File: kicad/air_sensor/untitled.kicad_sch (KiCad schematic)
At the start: 7 parts, among them J2 Micro_SD_Card

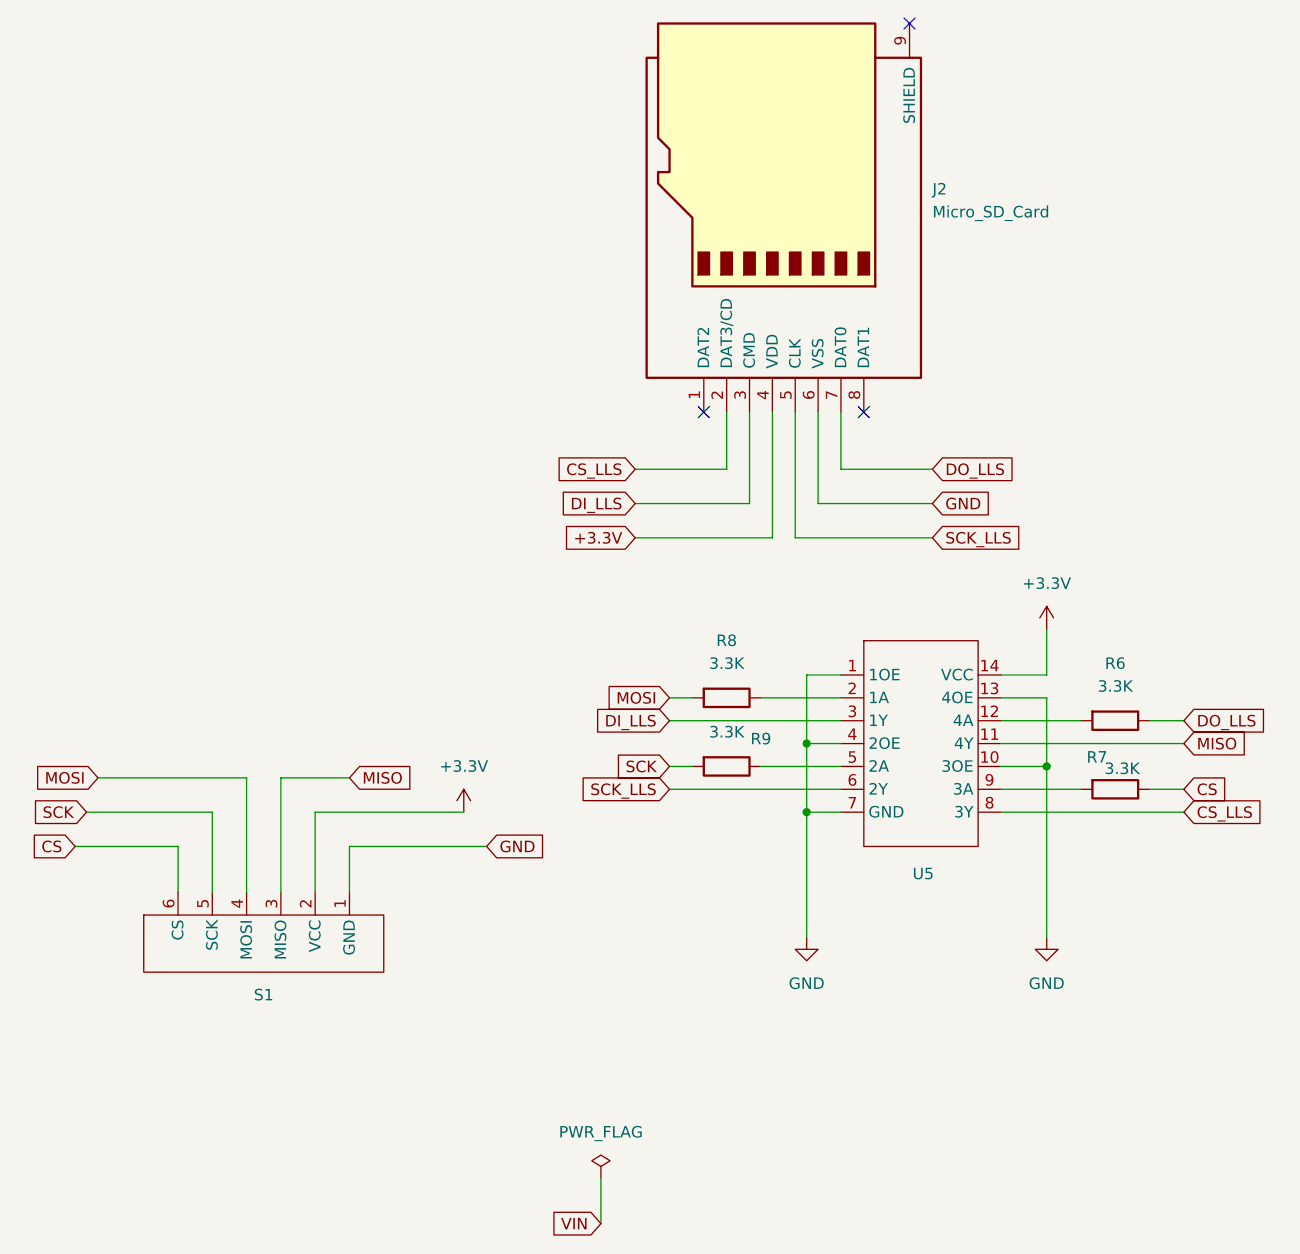
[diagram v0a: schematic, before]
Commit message: updated schema
added 5V 3A buck converter
refined 3v3 LDO
added symbols for new components
added text comments for designing the pcb
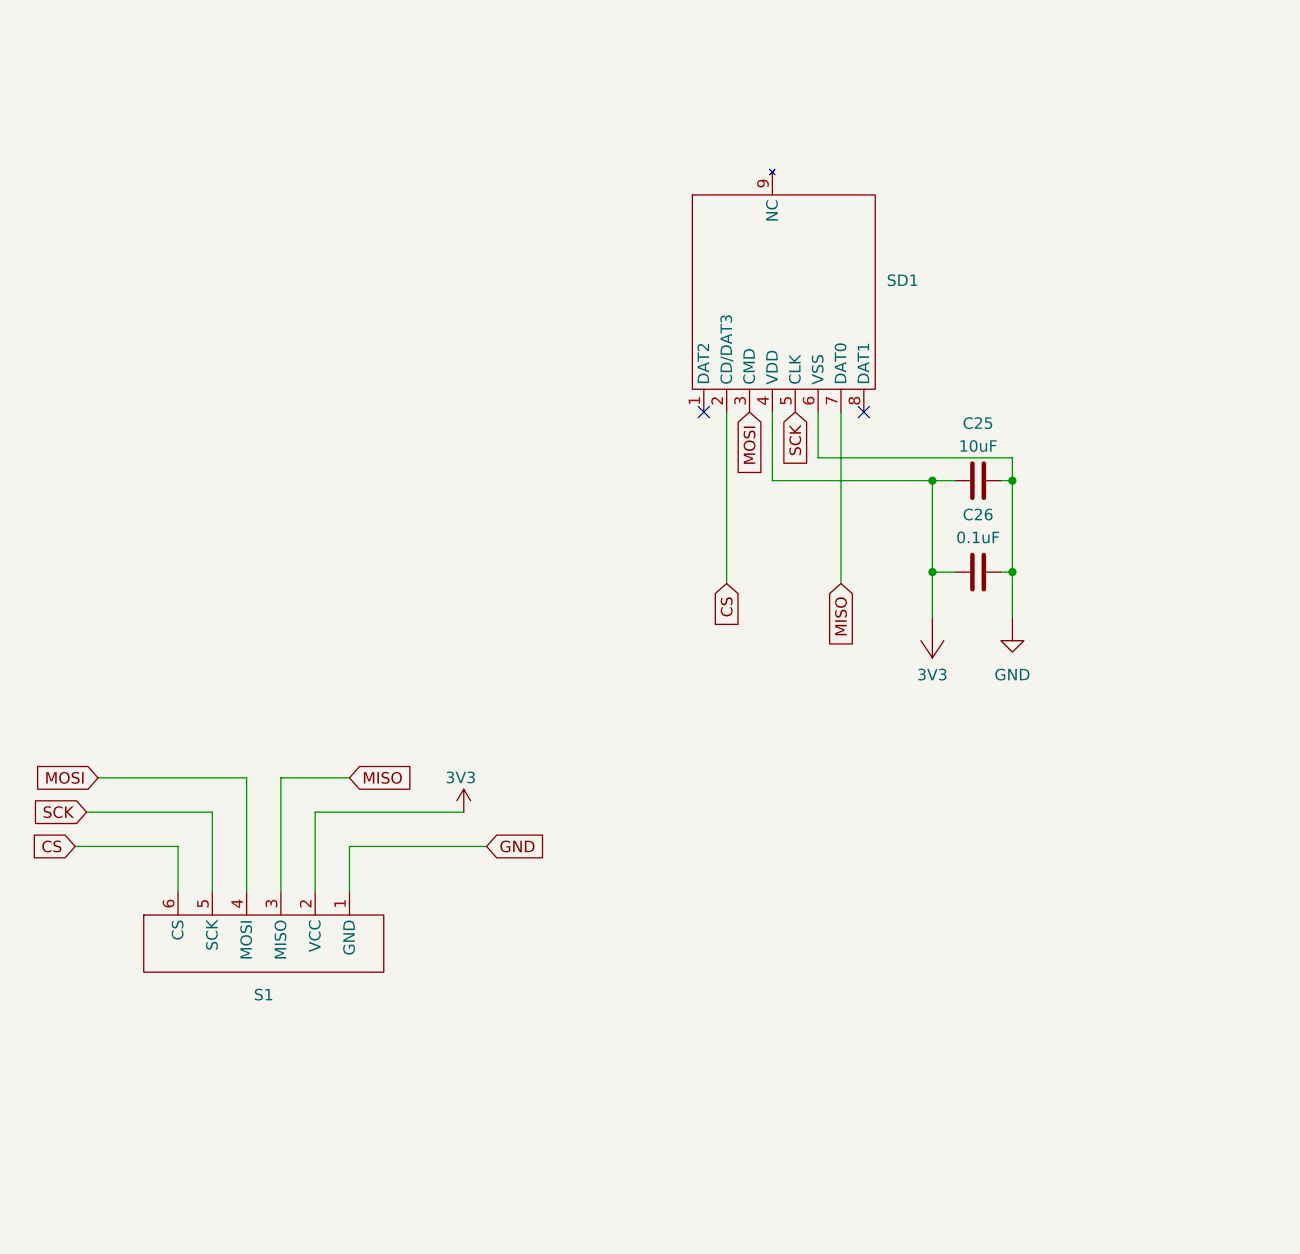
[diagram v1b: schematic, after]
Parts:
- removed J2: Micro_SD_Card, symbol Connector:Micro_SD_Card
- removed R6, R7, R8, R9: 3.3K, symbol Device:R
- removed U5: ~, symbol air_sens_lib:SN74LVC125
- added C25: 10uF, symbol common:Capacitor
- added C26: 0.1uF, symbol common:Capacitor
- added SD1: ~, symbol air_sens_lib:SD_SLOT
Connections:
- net CS: now also SD1.2 (CD/DAT3)
- net GND: now also C25.2, C26.2, SD1.6 (VSS)
- net MISO: now also SD1.7 (DAT0)
- net MOSI: now also SD1.3 (CMD)
- net SCK: now also SD1.5 (CLK)
- net +3.3V renamed 3V3
- net 3V3: now also C25.1, C26.1, SD1.4 (VDD)
- no-connect marks 3 -> 2

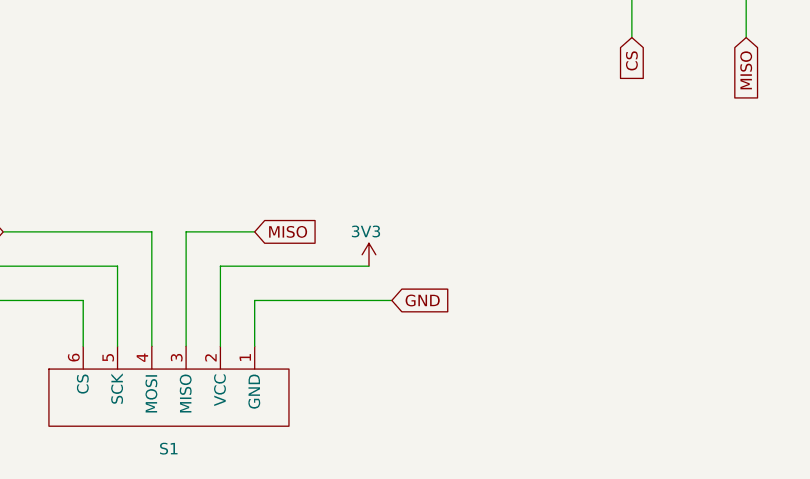
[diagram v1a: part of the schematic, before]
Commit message: updated power symbol labels, replaced power symbols in schematic with our own custom symbols
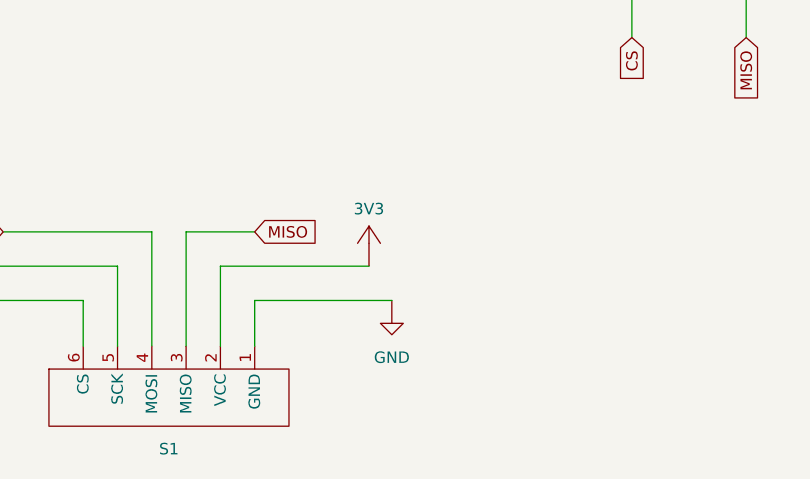
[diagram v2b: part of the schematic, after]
